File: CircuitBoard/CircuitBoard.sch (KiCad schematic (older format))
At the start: 14 parts, among them J1 MotorConnector, J2 PowerHeader1, J3 PowerHeader2, Q1 TIP31C, U1 LM555xN

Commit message: Finished OpenClinostat v1 Board
This update contains all of the schematics needed to print the V1 board.
The board is labled with all of the parts needed, and where all of the
wires should be connected.
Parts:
- C1: footprint (none) -> Capacitor_THT:C_Disc_D6.0mm_W2.5mm_P5.00mm
- C2, C3: footprint (none) -> Capacitor_THT:CP_Radial_D4.0mm_P2.00mm
- D1, D2, D3: footprint (none) -> Diode_THT:D_DO-35_SOD27_P7.62mm_Horizontal
- J1, J2, J3: footprint (none) -> Connector_PinHeader_2.54mm:PinHeader_1x02_P2.54mm_Vertical
- R1, R2: footprint (none) -> Resistor_THT:R_Axial_DIN0207_L6.3mm_D2.5mm_P7.62mm_Horizontal
- RV1: footprint (none) -> Connector_PinHeader_2.54mm:PinHeader_1x03_P2.54mm_Vertical
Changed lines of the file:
@@
 F 0 "RV1" H 5280 3604 50  0000 R CNN
 F 1 "100K" H 5280 3695 50  0000 R CNN
-F 2 "" H 5350 3650 50  0001 C CNN
+F 2 "Connector_PinHeader_2.54mm:PinHeader_1x03_P2.54mm_Vertical" H 5350 3650 50  0001 C CNN
 F 3 "~" H 5350 3650 50  0001 C CNN
 	1    5350 3650
@@
 F 0 "D2" H 5300 3117 50  0000 C CNN
 F 1 "1N4148" H 5300 3026 50  0000 C CNN
-F 2 "" H 5300 2900 50  0001 C CNN
+F 2 "Diode_THT:D_DO-35_SOD27_P7.62mm_Horizontal" H 5300 2900 50  0001 C CNN
 F 3 "~" H 5300 2900 50  0001 C CNN
 	1    5300 2900
@@
 F 0 "D3" H 5300 2983 50  0000 C CNN
 F 1 "1N4148" H 5300 3074 50  0000 C CNN
-F 2 "" H 5300 3200 50  0001 C CNN
+F 2 "Diode_THT:D_DO-35_SOD27_P7.62mm_Horizontal" H 5300 3200 50  0001 C CNN
 F 3 "~" H 5300 3200 50  0001 C CNN
 	1    5300 3200
@@
 F 0 "R1" H 4770 2646 50  0000 L CNN
 F 1 "1k" H 4770 2555 50  0000 L CNN
-F 2 "" V 4630 2600 50  0001 C CNN
+F 2 "Resistor_THT:R_Axial_DIN0207_L6.3mm_D2.5mm_P7.62mm_Horizontal" V 4630 2600 50  0001 C CNN
 F 3 "~" H 4700 2600 50  0001 C CNN
 	1    4700 2600
@@
 F 0 "R2" H 5120 2646 50  0000 L CNN
 F 1 "10k" H 5120 2555 50  0000 L CNN
-F 2 "" V 4980 2600 50  0001 C CNN
+F 2 "Resistor_THT:R_Axial_DIN0207_L6.3mm_D2.5mm_P7.62mm_Horizontal" V 4980 2600 50  0001 C CNN
 F 3 "~" H 5050 2600 50  0001 C CNN
 	1    5050 2600
@@
 F 0 "C1" H 2515 2446 50  0000 L CNN
 F 1 ".1mf" H 2515 2355 50  0000 L CNN
-F 2 "" H 2438 2250 50  0001 C CNN
+F 2 "Capacitor_THT:C_Disc_D6.0mm_W2.5mm_P5.00mm" H 2438 2250 50  0001 C CNN
 F 3 "~" H 2400 2400 50  0001 C CNN
 	1    2400 2400
@@
 F 0 "C3" H 3182 2354 50  0000 R CNN
 F 1 ".1mf" H 3182 2445 50  0000 R CNN
-F 2 "" H 3338 2250 50  0001 C CNN
+F 2 "Capacitor_THT:CP_Radial_D4.0mm_P2.00mm" H 3338 2250 50  0001 C CNN
 F 3 "~" H 3300 2400 50  0001 C CNN
 	1    3300 2400
@@
 F 0 "C2" H 2782 2354 50  0000 R CNN
 F 1 ".1mf" H 2782 2445 50  0000 R CNN
-F 2 "" H 2938 2250 50  0001 C CNN
+F 2 "Capacitor_THT:CP_Radial_D4.0mm_P2.00mm" H 2938 2250 50  0001 C CNN
 F 3 "~" H 2900 2400 50  0001 C CNN
 	1    2900 2400
@@
 F 0 "J2" H 1818 1925 50  0000 C CNN
 F 1 "PowerHeader1" H 1818 2016 50  0000 C CNN
-F 2 "" H 1900 2250 50  0001 C CNN
+F 2 "Connector_PinHeader_2.54mm:PinHeader_1x02_P2.54mm_Vertical" H 1900 2250 50  0001 C CNN
 F 3 "~" H 1900 2250 50  0001 C CNN
 	1    1900 2250
@@
 F 0 "J3" H 1818 2325 50  0000 C CNN
 F 1 "PowerHeader2" H 1818 2416 50  0000 C CNN
-F 2 "" H 1900 2650 50  0001 C CNN
+F 2 "Connector_PinHeader_2.54mm:PinHeader_1x02_P2.54mm_Vertical" H 1900 2650 50  0001 C CNN
 F 3 "~" H 1900 2650 50  0001 C CNN
 	1    1900 2650
@@
 F 0 "J1" H 5680 1542 50  0000 L CNN
 F 1 "MotorConnector" H 5680 1451 50  0000 L CNN
-F 2 "" H 5600 1550 50  0001 C CNN
+F 2 "Connector_PinHeader_2.54mm:PinHeader_1x02_P2.54mm_Vertical" H 5600 1550 50  0001 C CNN
 F 3 "~" H 5600 1550 50  0001 C CNN
 	1    5600 1550
@@
 F 0 "D1" H 5150 1767 50  0000 C CNN
 F 1 "1N4148" H 5150 1676 50  0000 C CNN
-F 2 "" H 5150 1550 50  0001 C CNN
+F 2 "Diode_THT:D_DO-35_SOD27_P7.62mm_Horizontal" H 5150 1550 50  0001 C CNN
 F 3 "~" H 5150 1550 50  0001 C CNN
 	1    5150 1550

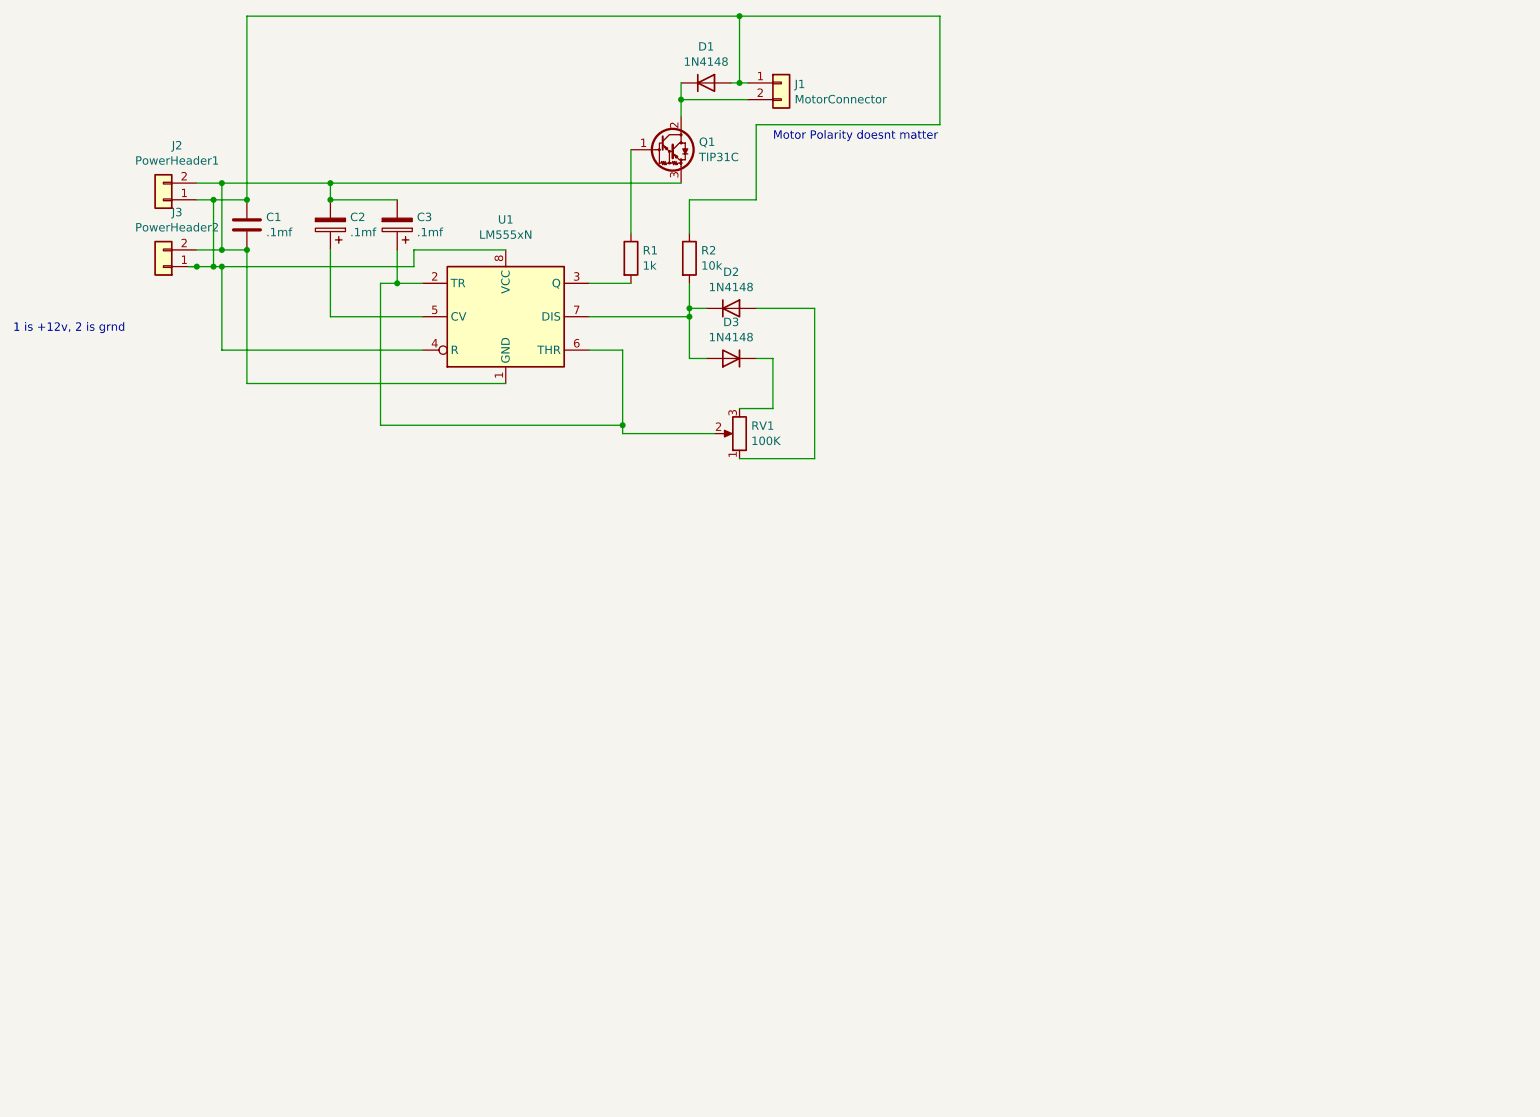
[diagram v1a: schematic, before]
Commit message: Fixed an issue in the V1 Board
New files in the 'second try' folder.
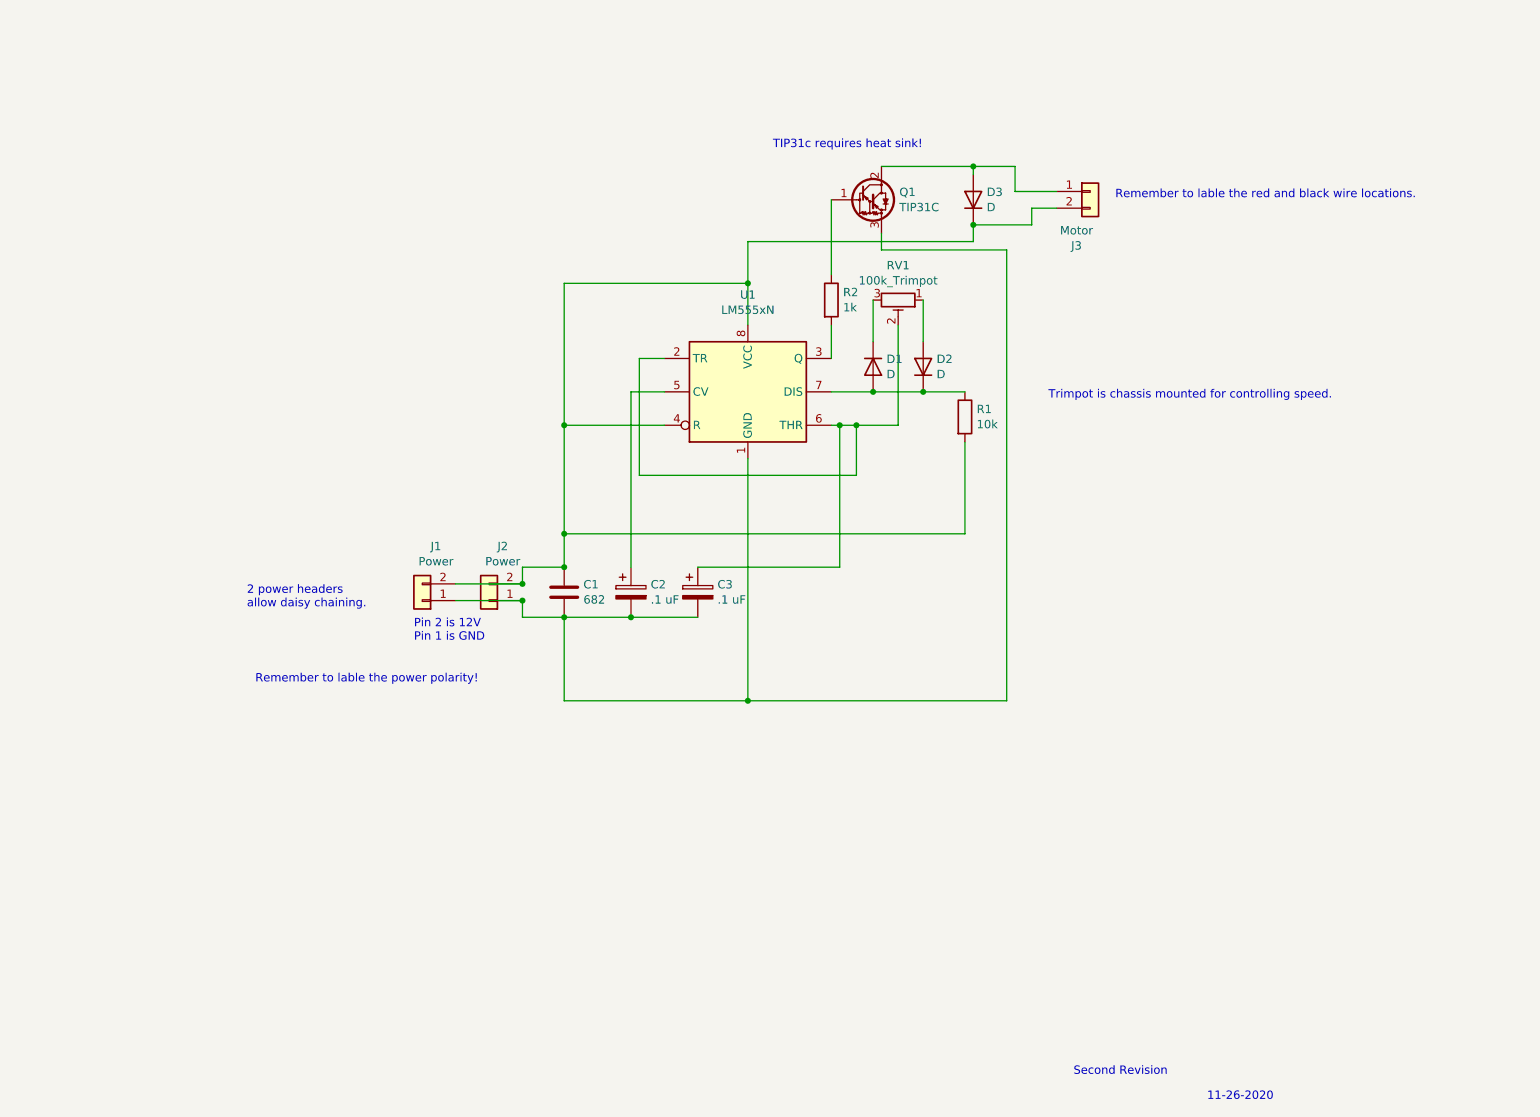
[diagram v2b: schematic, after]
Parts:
- removed RV1: 100K, Connector_PinHeader_2.54mm:PinHeader_1x03_P2.54mm_Vertical, symbol Device:R_POT
- added RV1: 100k_Trimpot, Connector_PinHeader_2.00mm:PinHeader_1x03_P2.00mm_Vertical, symbol Device:R_POT_TRIM
- C1: value .1mf -> 682; footprint Capacitor_THT:C_Disc_D6.0mm_W2.5mm_P5.00mm -> Capacitor_THT:C_Disc_D8.0mm_W2.5mm_P5.00mm
- C2, C3: value .1mf -> .1 uF
- D1, D2, D3: value 1N4148 -> D; footprint Diode_THT:D_DO-35_SOD27_P7.62mm_Horizontal -> Diode_THT:D_DO-35_SOD27_P5.08mm_Vertical_AnodeUp
- J1: value MotorConnector -> Power; footprint Connector_PinHeader_2.54mm:PinHeader_1x02_P2.54mm_Vertical -> Connector_PinHeader_2.00mm:PinHeader_1x02_P2.00mm_Vertical
- J2: value PowerHeader1 -> Power; footprint Connector_PinHeader_2.54mm:PinHeader_1x02_P2.54mm_Vertical -> Connector_PinHeader_2.00mm:PinHeader_1x02_P2.00mm_Vertical
- J3: value PowerHeader2 -> Motor; footprint Connector_PinHeader_2.54mm:PinHeader_1x02_P2.54mm_Vertical -> Connector_PinHeader_2.00mm:PinHeader_1x02_P2.00mm_Vertical
- R1: value 1k -> 10k; footprint Resistor_THT:R_Axial_DIN0207_L6.3mm_D2.5mm_P7.62mm_Horizontal -> Resistor_THT:R_Axial_DIN0207_L6.3mm_D2.5mm_P10.16mm_Horizontal
- R2: value 10k -> 1k; footprint Resistor_THT:R_Axial_DIN0207_L6.3mm_D2.5mm_P7.62mm_Horizontal -> Resistor_THT:R_Axial_DIN0207_L6.3mm_D2.5mm_P10.16mm_Horizontal
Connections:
- net at D2.2 (A): now also RV1.1
- net at C3.1, U1.2 (TR), U1.6 (THR): now also RV1.2
- net at D3.1 (K): now also C1.1, J1.2 (Pin_2), J2.2 (Pin_2), J3.2 (Pin_2), R1.2, U1.4 (R), U1.8 (VCC)
- net at C1.2, C2.2, C3.2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: now also J1.1 (Pin_1), J2.1 (Pin_1); no longer J2.2 (Pin_2), J3.2 (Pin_2)
- net at U1.3 (Q): now also R2.2; no longer R1.2
- net at D2.1 (K), U1.7 (DIS): now also D1.2 (A), R1.1; no longer D3.2 (A), R2.2
- net at Q1.1 (B): now also R2.1; no longer R1.1
- new net: D1.1 (K), RV1.3
- new net: D3.2 (A), J3.1 (Pin_1), Q1.2 (C)
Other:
- note added: "11-26-2020\n"
- note added: "2 power headers\nallow daisy chaining."
- note added: "Pin 2 is 12V\nPin 1 is GND"
- note added: "Remember to lable the power polarity!"
- note added: "Remember to lable the red and black wire locations.\n"
- note added: "Second Revision"
- note added: "TIP31c requires heat sink!"
- note added: "Trimpot is chassis mounted for controlling speed."
- note removed: "1 is +12v, 2 is grnd"
- note removed: "Motor Polarity doesnt matter"
